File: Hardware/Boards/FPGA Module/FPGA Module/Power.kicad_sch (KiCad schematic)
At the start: 165 parts, among them U10 L78L33_SOT89, U11 INA236, U12 TMP1075DSG, U13 INA700AYWFR, U15 INA700AYWFR, U17 INA700AYWFR, U19 INA700AYWFR, U24 MP8796, U25 MP8796, U6 TMP1075DSG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

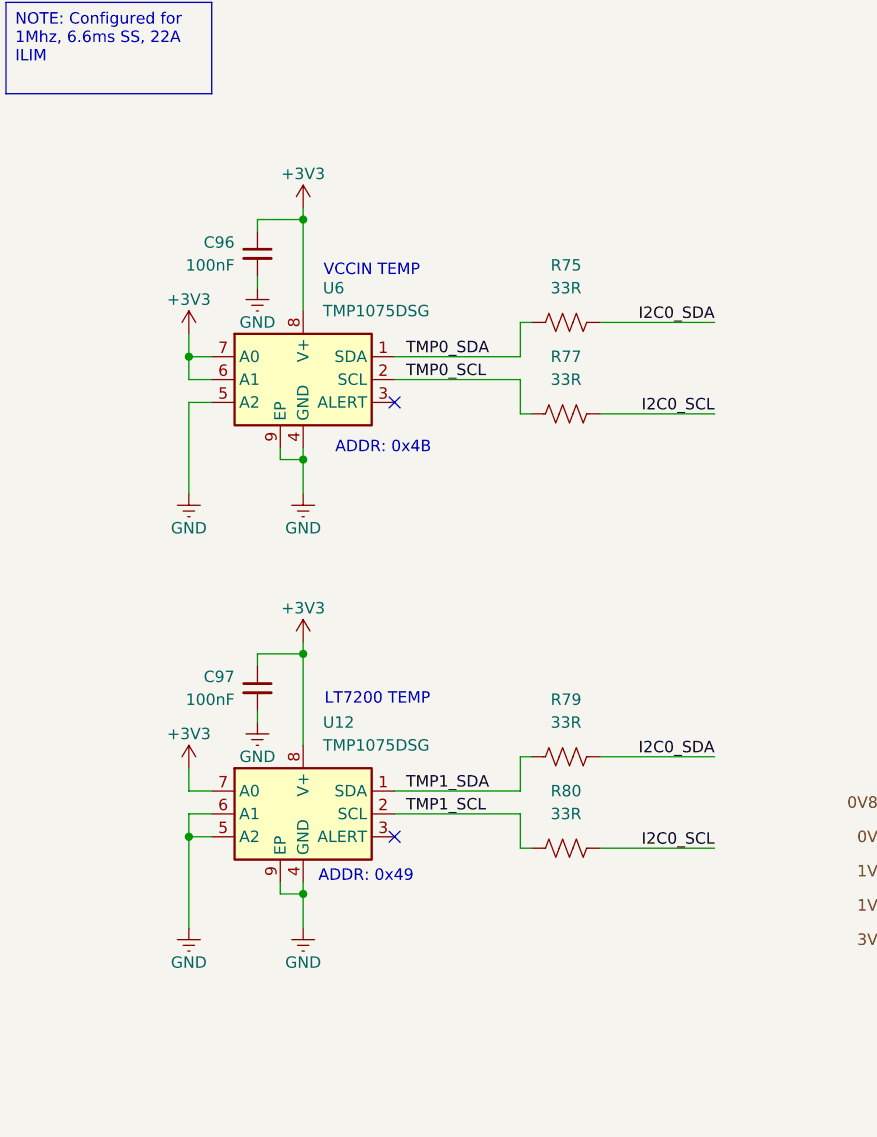
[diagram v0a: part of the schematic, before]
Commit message: Fixed FPGA Module Routing
Reversed B2B headers and re-routed connections to FPGA
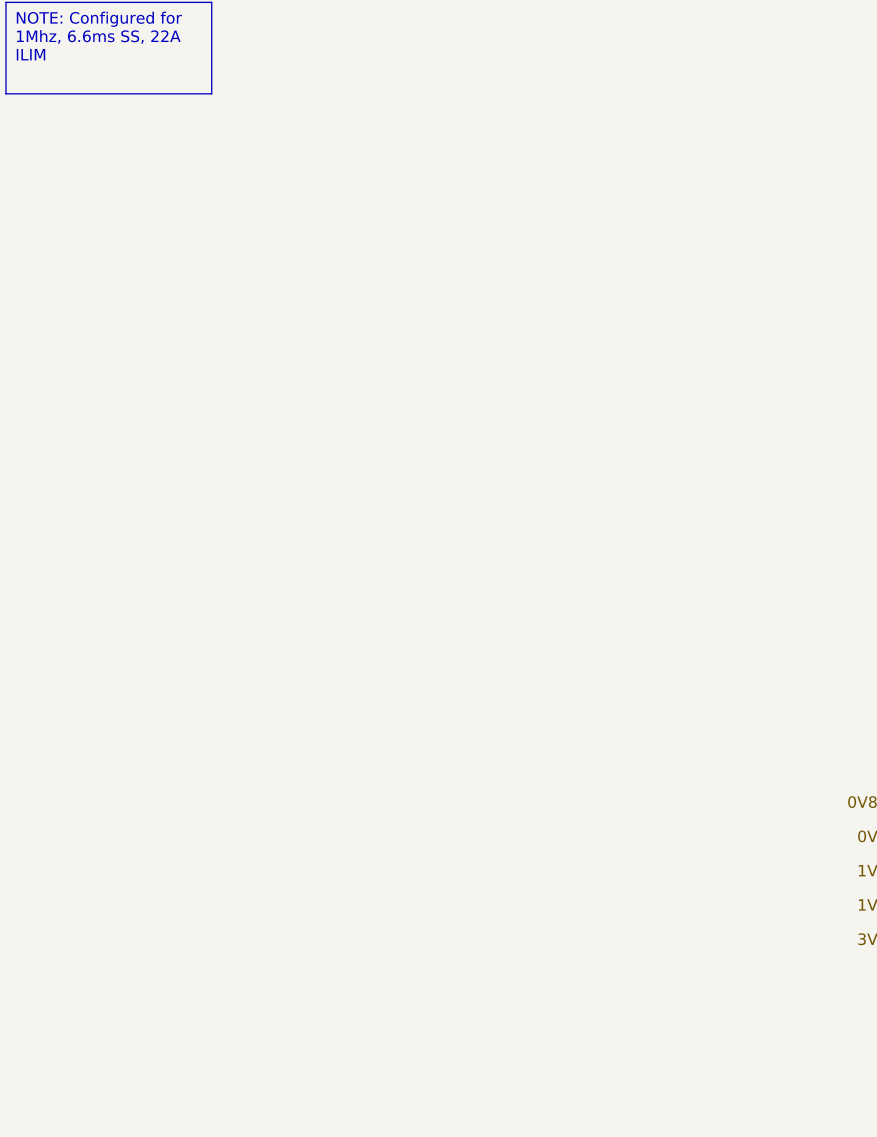
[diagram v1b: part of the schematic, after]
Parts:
- removed C96, C97: 100nF, Capacitor_SMD:C_0201_0603Metric, symbol Device:C_Small
- removed R75, R77, R79, R80: 33R, Resistor_SMD:R_0201_0603Metric, symbol Device:R_US
- removed U12, U6: TMP1075DSG, Package_SON:WSON-8-1EP_2x2mm_P0.5mm_EP0.9x1.6mm_ThermalVias, symbol Sensor_Temperature:TMP1075DSG
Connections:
- no-connect marks 3 -> 1
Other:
- note removed: "ADDR: 0x49"
- note removed: "ADDR: 0x4B"
- note removed: "LT7200 TEMP"
- note removed: "VCCIN TEMP"

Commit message: Generated FPGA module gerbers
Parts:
- TP28, TP33, TP36, TP39, TP42, TP43, TP44, TP45, TP46, TP47: footprint FPGA Module:Test Point 0.75mm -> FPGA Module:Test Point 0.5mm No Silk
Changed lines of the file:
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@@
 			)
 		)
-		(property "Footprint" "FPGA Module:Test Point 0.75mm"
+		(property "Footprint" "FPGA Module:Test Point 0.5mm No Silk"
 			(at 228.6 351.79 0)
 			(effects
@@
 			)
 		)
-		(property "Footprint" "FPGA Module:Test Point 0.75mm"
+		(property "Footprint" "FPGA Module:Test Point 0.5mm No Silk"
 			(at 218.44 351.79 0)
 			(effects
@@
 			)
 		)
-		(property "Footprint" "FPGA Module:Test Point 0.75mm"
+		(property "Footprint" "FPGA Module:Test Point 0.5mm No Silk"
 			(at 208.28 351.79 0)
 			(effects
@@
 			)
 		)
-		(property "Footprint" "FPGA Module:Test Point 0.75mm"
+		(property "Footprint" "FPGA Module:Test Point 0.5mm No Silk"
 			(at 511.81 219.71 0)
 			(effects
@@
 			)
 		)
-		(property "Footprint" "FPGA Module:Test Point 0.75mm"
+		(property "Footprint" "FPGA Module:Test Point 0.5mm No Silk"
 			(at 187.96 351.79 0)
 			(effects
@@
 			)
 		)
-		(property "Footprint" "FPGA Module:Test Point 0.75mm"
+		(property "Footprint" "FPGA Module:Test Point 0.5mm No Silk"
 			(at 510.54 265.43 0)
 			(effects
@@
 			)
 		)
-		(property "Footprint" "FPGA Module:Test Point 0.75mm"
+		(property "Footprint" "FPGA Module:Test Point 0.5mm No Silk"
 			(at 509.27 308.61 0)
 			(effects
@@
 			)
 		)
-		(property "Footprint" "FPGA Module:Test Point 0.75mm"
+		(property "Footprint" "FPGA Module:Test Point 0.5mm No Silk"
 			(at 288.29 41.91 0)
 			(effects
@@
 			)
 		)
-		(property "Footprint" "FPGA Module:Test Point 0.75mm"
+		(property "Footprint" "FPGA Module:Test Point 0.5mm No Silk"
 			(at 511.81 175.26 0)
 			(effects
@@
 			)
 		)
-		(property "Footprint" "FPGA Module:Test Point 0.75mm"
+		(property "Footprint" "FPGA Module:Test Point 0.5mm No Silk"
 			(at 198.12 351.79 0)
 			(effects

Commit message: Updates to sch
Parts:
- C160: value 220nF -> 470nF
- R133: value 20K -> 12K
- R134: value 47K -> 27K
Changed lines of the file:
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@@
 			)
 		)
-		(property "Value" "47K"
+		(property "Value" "27K"
 			(at 128.27 76.1999 0)
 			(effects
@@
 			)
 		)
-		(property "Value" "220nF"
+		(property "Value" "470nF"
 			(at 82.55 134.6262 0)
 			(effects
@@
 			)
 		)
-		(property "Value" "20K"
+		(property "Value" "12K"
 			(at 128.27 66.0399 0)
 			(effects
